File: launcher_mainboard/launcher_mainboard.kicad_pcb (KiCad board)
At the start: 4 copper layers, 83 x 102 mm, 83 parts, among them J1 USB_C_Receptacle_USB2.0_16P, J10 header, J11 header, J2 Conn_01x06, J3 Conn_01x06, J4 Conn_01x06, J5 Conn_01x06, J6 bat_con, J7 fan_con, J8 ESC_1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

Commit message: more layout
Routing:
- net -BATT: track 199.9 -> 200.0 mm, vias 31 -> 32
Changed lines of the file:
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@@
 		(tags "resistor")
 		(property "Reference" "R17"
-			(at -3.5875 0 180)
+			(at -2.80625 -0.0375 180)
 			(layer "F.SilkS")
 			(effects
@@
 		(tags "SOT TO_SOT_SMD")
 		(property "Reference" "Q5"
-			(at 0 3.07 0)
+			(at -0.0375 2.61875 0)
 			(layer "F.SilkS")
 			(effects
@@
 		(tags "resistor")
 		(property "Reference" "R15"
-			(at -3.2325 0 180)
+			(at -2.73125 0 180)
 			(layer "F.SilkS")
 			(effects
@@
 		(tags "resistor")
 		(property "Reference" "R18"
-			(at -3.5 0 180)
+			(at -2.81875 0 180)
 			(layer "F.SilkS")
 			(effects
@@
 		(tags "resistor")
 		(property "Reference" "R19"
-			(at -3.5 0 180)
+			(at -2.81875 -1.0375 180)
 			(layer "F.SilkS")
 			(effects
@@
 		(tags "SOT TO_SOT_SMD")
 		(property "Reference" "Q6"
-			(at 0 3.07 0)
+			(at 0 2.91875 0)
 			(layer "F.SilkS")
 			(effects
@@
 		(tags "resistor")
 		(property "Reference" "R20"
-			(at -3.5 0 180)
+			(at -3.01875 0.5625 180)
 			(layer "F.SilkS")
 			(effects
@@
 	)
 	(segment
+		(start 99.4 100.4)
+		(end 95.60625 100.4)
+		(width 0.254)
+		(layer "F.Cu")
+		(net 1)
+	)
+	(segment
+		(start 99.6 100.4)
+		(end 99.5 100.5)
+		(width 0.254)
+		(layer "F.Cu")
+		(net 1)
+	)
+	(segment
 		(start 113 107.35)
 		(end 109.525 107.35)
@@
 	)
 	(segment
+		(start 99.5 100.5)
+		(end 99.4 100.4)
+		(width 0.254)
+		(layer "F.Cu")
+		(net 1)
+	)
+	(segment
 		(start 91.1 99.7)
 		(end 91.120146 99.679854)
@@
 	(segment
 		(start 99.74375 100.4)
-		(end 95.60625 100.4)
+		(end 99.6 100.4)
 		(width 0.254)
 		(layer "F.Cu")
@@
 	)
 	(via
+		(at 99.5 100.5)
+		(size 0.6)
+		(drill 0.2)
+		(layers "F.Cu" "B.Cu")
+		(net 1)
+	)
+	(via
 		(at 153.5 54)
 		(size 0.7)
@@
 	)
 	(segment
-		(start 102.6 102.9)
-		(end 102.6 102.9)
-		(width 0.25)
-		(layer "F.Cu")
-		(net 4)
-	)
-	(segment
 		(start 118.5 93)
 		(end 118.5 92.9)
@@
 	)
 	(segment
-		(start 102.6 102.9)
-		(end 102.5 102.9)
-		(width 0.25)
-		(layer "F.Cu")
-		(net 4)
-	)
-	(segment
 		(start 88.23125 62.7)
 		(end 88.23125 65.225)
@@
 	)
 	(segment
-		(start 102.5 102.9)
-		(end 102.5 102.8)
-		(width 0.25)
-		(layer "F.Cu")
-		(net 4)
-	)
-	(segment
 		(start 88.31875 93.575)
 		(end 88.44375 93.7)
@@
 	)
 	(segment
-		(start 102.5 102.8)
-		(end 103 103.3)
+		(start 102.5 103.3)
+		(end 103.575063 103.3)
 		(width 0.25)
 		(layer "F.Cu")
@@
 	)
 	(segment
-		(start 103 103.3)
-		(end 103.575063 103.3)
+		(start 102.6 103.2)
+		(end 102.5 103.3)
 		(width 0.25)
 		(layer "F.Cu")
@@
 	)
 	(via
-		(at 102.5 102.9)
+		(at 102.5 103.3)
 		(size 0.6)
 		(drill 0.2)

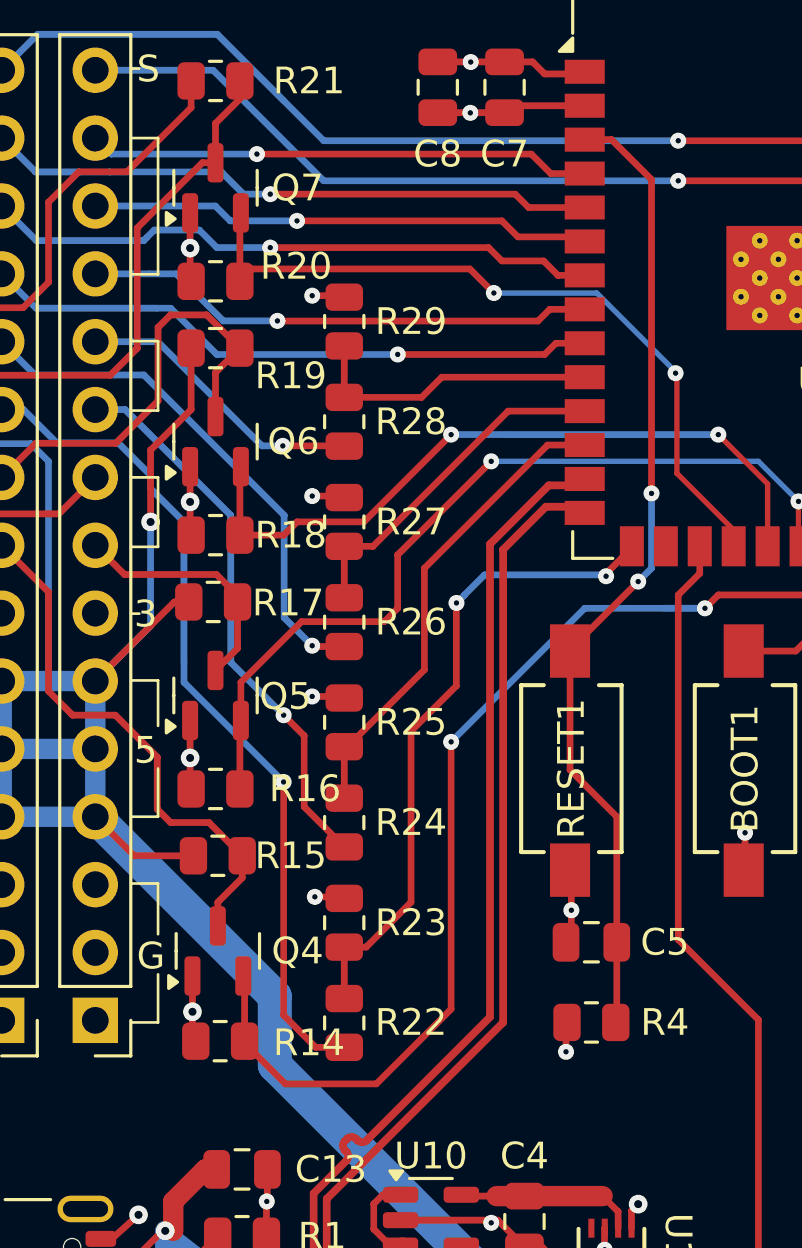
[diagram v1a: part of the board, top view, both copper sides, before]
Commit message: shifted over some resisters
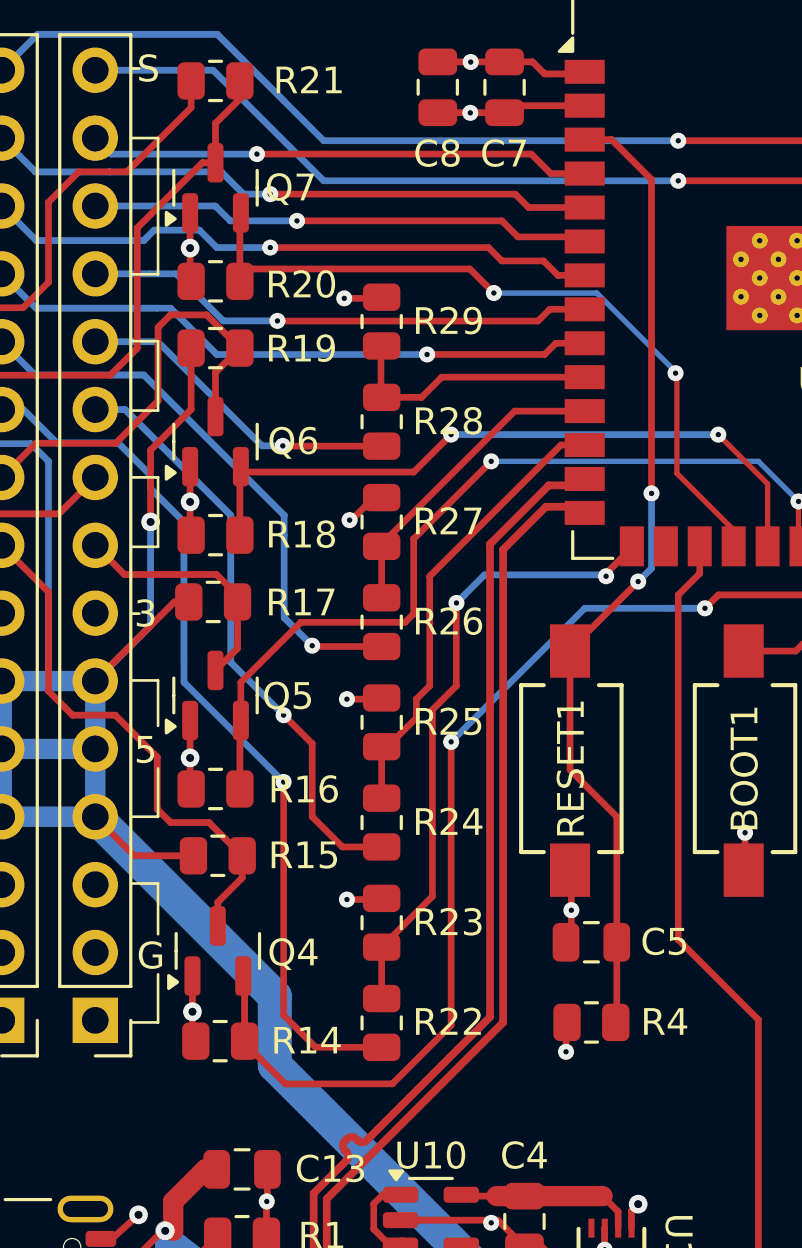
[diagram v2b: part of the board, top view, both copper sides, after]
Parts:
- moved R22 1.40 mm to (95.4, 93.0)
- moved R23 1.40 mm to (95.4, 89.3)
- moved R24 1.40 mm to (95.4, 85.5)
- moved R25 1.40 mm to (95.4, 81.8)
- moved R26 1.40 mm to (95.4, 78.0)
- moved R27 1.40 mm to (95.4, 74.3)
- moved R28 1.40 mm to (95.4, 70.5)
- moved R29 1.40 mm to (95.4, 66.8)
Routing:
- net /HV_SIGNAL_3: track 19.9 -> 21.4 mm
- net /HV_SIGNAL_2: track 20.9 -> 22.3 mm
- net /HV_SIGNAL_4: track 10.9 -> 12.3 mm
- net /HV_SIGNAL_1: track 31.6 -> 33.0 mm
- net /LV_SIGNAL_4: track 11.2 -> 9.86 mm
- net /LV_SIGNAL_3: track 13.0 -> 11.7 mm
- net /LV_SIGNAL_1: track 24.7 -> 23.6 mm
- net /LV3: track 27.0 -> 26.1 mm
- net /LV_SIGNAL_2: track 17.8 -> 17.0 mm
- net -BATT: track 200.0 -> 200.6 mm

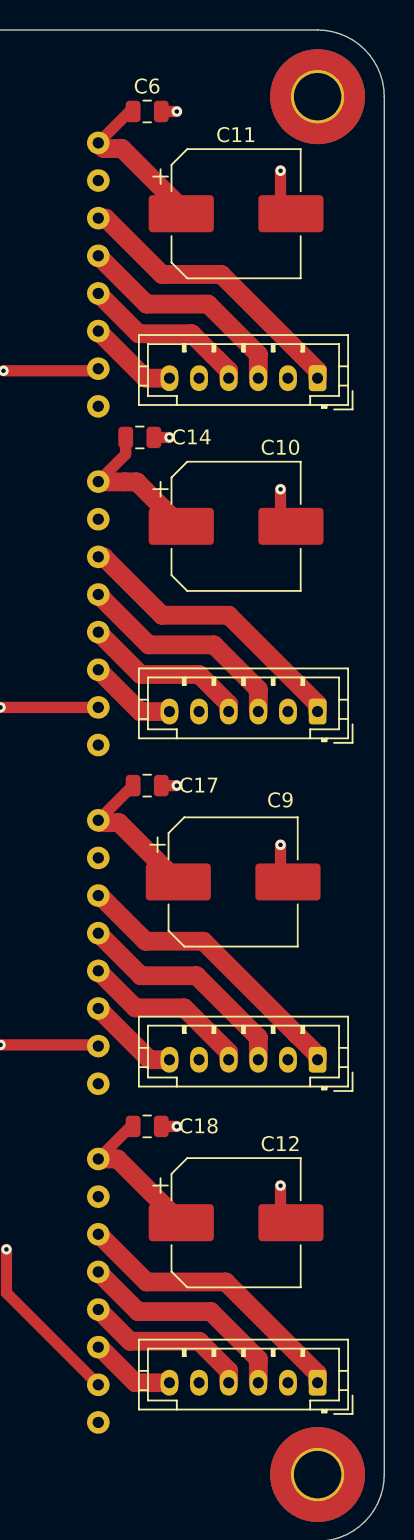
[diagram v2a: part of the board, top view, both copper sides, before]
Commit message: switch stepper connector to XH
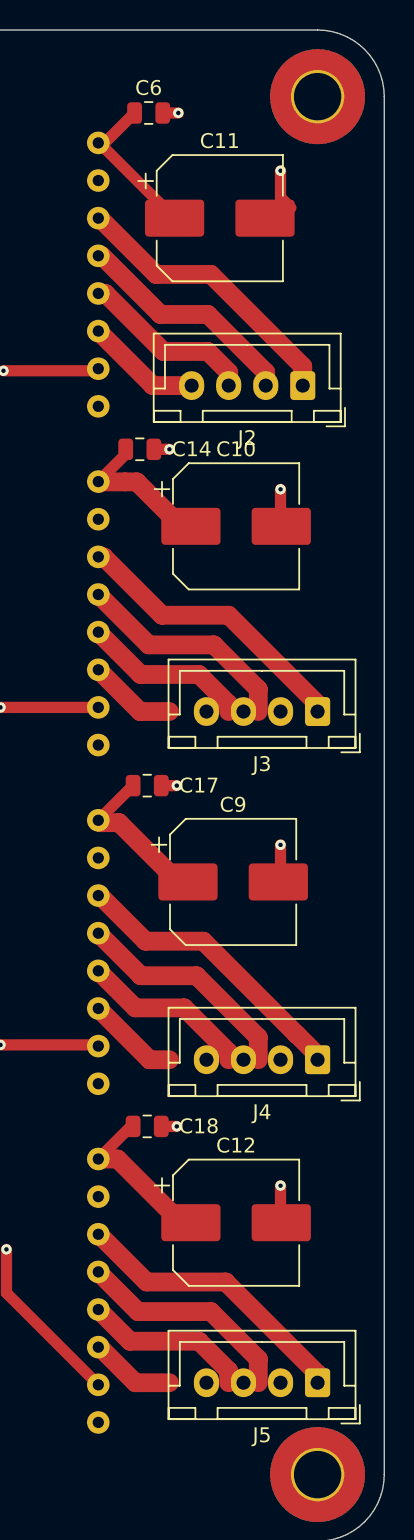
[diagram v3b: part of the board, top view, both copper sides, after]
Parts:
- C10, C11, C12, C9: footprint Capacitor_SMD:CP_Elec_8x10.5 -> Capacitor_SMD:CP_Elec_8x6.7
- J2, J3, J4, J5: value Conn_01x06 -> Conn_01x04; footprint Connector_JST:JST_PH_B6B-PH-K_1x06_P2.00mm_Vertical -> Connector_JST:JST_XH_B4B-XH-A_1x04_P2.50mm_Vertical
- moved C11 1.14 mm to (149.4, 57.2)
- moved J2 1.12 mm to (155.0, 68.5)
- moved C14 0.80 mm to (144.0, 72.8)
- moved C6 0.14 mm to (144.6, 50.1)
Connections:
- J2 pad 2: unconnected-(J2-Pin_2-Pad2) -> /M1_A1
- J2 pad 3: /M1_A1 -> /M1_B1
- J2 pad 4: /M1_B1 -> /M1_B2
- J3 pad 2: unconnected-(J3-Pin_2-Pad2) -> /M2_A1
- J3 pad 3: /M2_A1 -> /M2_B1
- J3 pad 4: /M2_B1 -> /M2_B2
- J4 pad 2: unconnected-(J4-Pin_2-Pad2) -> /M3_A1
- J4 pad 3: /M3_A1 -> /M3_B1
- J4 pad 4: /M3_B1 -> /M3_B2
- J5 pad 2: unconnected-(J5-Pin_2-Pad2) -> /M4_A1
- J5 pad 3: /M4_A1 -> /M4_B1
- J5 pad 4: /M4_B1 -> /M4_B2
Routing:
- net /M1_B2: track 6.12 -> 7.82 mm
- net +BATT: track 193.9 -> 192.6 mm

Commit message: flipped ESD IC, selected zener diode and updated footprint
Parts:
- D2: footprint Diode_SMD:D_0805_2012Metric -> Diode_SMD:D_SOD-123
- moved J3 2.51 mm to (155.0, 88.2)
- moved J4 1.93 mm to (155.1, 112.3)
- moved J5 1.12 mm to (155.0, 135.3)
- moved D2 0.69 mm to (113.1, 107.1)
- moved C11 0.63 mm to (149.6, 56.6)
- turned D3 to 0 degrees
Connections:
- D3 pad 1: /USB_D+ -> /USB_D-
- D3 pad 3: /USB_D- -> /USB_D+
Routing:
- net /+5VUSB: track 31.0 -> 17.8 mm
- net +BATT: track 192.6 -> 184.9 mm
- net -BATT: track 200.6 -> 196.6 mm
- net /M4_B2: track 5.79 -> 7.09 mm
- net /USB_D+: track 46.3 -> 47.6 mm
- net /M2_A2: track 19.4 -> 18.3 mm
- net /M3_B2: track 6.23 -> 7.09 mm
- net /M3_A2: track 19.6 -> 18.8 mm
- net /M2_B1: track 11.3 -> 10.6 mm
- net /M2_A1: track 15.0 -> 14.3 mm
- net /USB_D-: track 46.9 -> 47.5 mm
- net /+3.3VBatt: track 15.9 -> 15.3 mm
- net /M2_B2: track 5.97 -> 6.52 mm
- added copper zone on B.Cu, net /+5VUSB

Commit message: finished up diode stuff
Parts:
- D1: value POWER_LED -> GREEN_LED
- D4: value INDICATOR_LED_1 -> RED_LED_1
- D5: value INDICATOR_LED_2 -> BLUE_LED_2
- D6: value 1N4004 -> SD103AW-TP; footprint Diode_SMD:D_0805_2012Metric -> Diode_SMD:D_SOD-123
- R10, R3: value 200 -> 100
- R12: value 200 -> 20
- moved D6 0.70 mm to (113.5, 99.8)
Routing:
- net +BATT: track 184.9 -> 180.5 mm
- net Net-(D6-A): track 10.7 -> 9.86 mm

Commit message: ordered board
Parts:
- R7: value 4k -> 3.9k
- moved C5 33.0 mm to (95.0, 58.0), turned to 90 degrees
- moved R4 1.50 mm to (102.5, 91.7), turned to -90 degrees
- moved R5 0.29 mm to (124.5, 59.3)
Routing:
- net Net-(U6-EN): track 36.7 -> 43.7 mm
- net -BATT: track 196.6 -> 200.8 mm, vias 32 -> 46
- net +3.3V: track 60.2 -> 61.1 mm
- net +BATT: track 180.5 -> 180.0 mm, vias 1 -> 0
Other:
- board text added: "BOOT"
- board text added: "RESET"
